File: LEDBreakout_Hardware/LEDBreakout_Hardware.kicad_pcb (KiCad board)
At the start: 2 copper layers, 39.9 x 39.9 mm, 29 parts, among them Q1 BSS138, Q2 BSS138, Q3 BSS138, Q4 BSS138

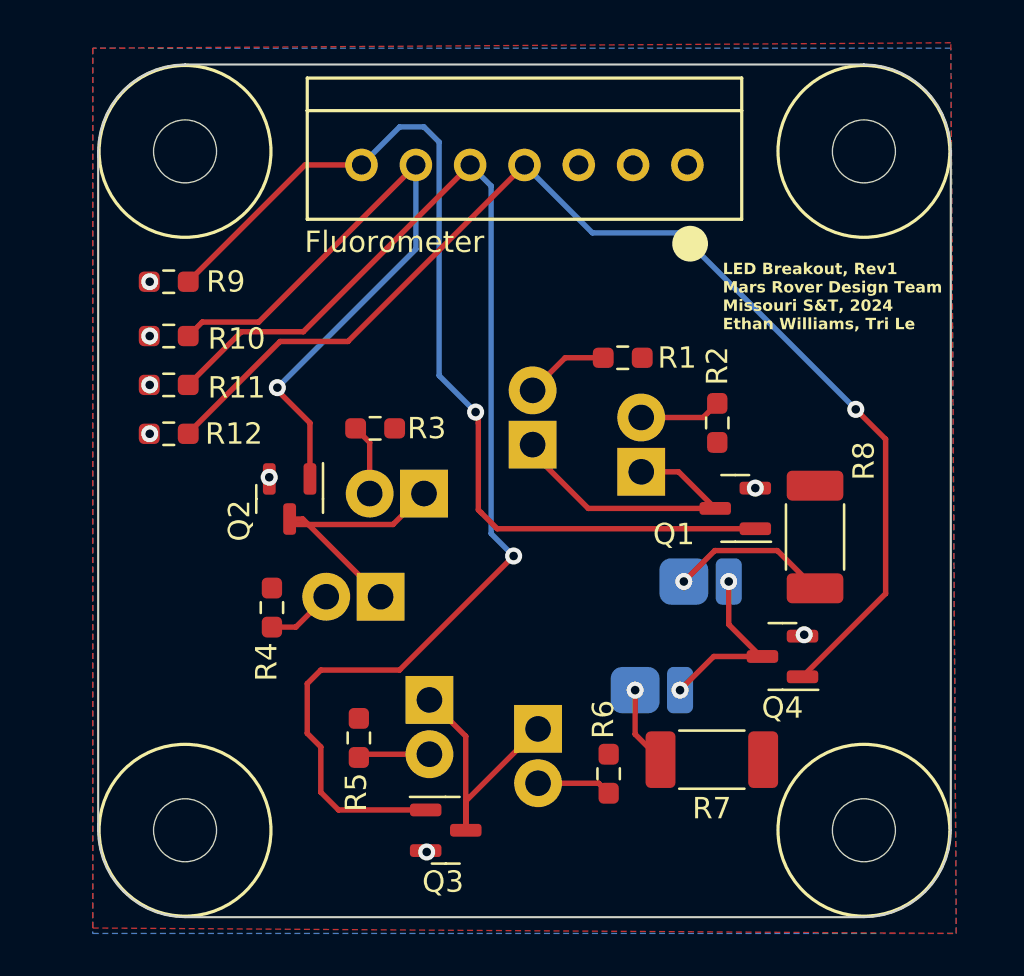
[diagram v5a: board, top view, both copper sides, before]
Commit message: Moved Vias off pads
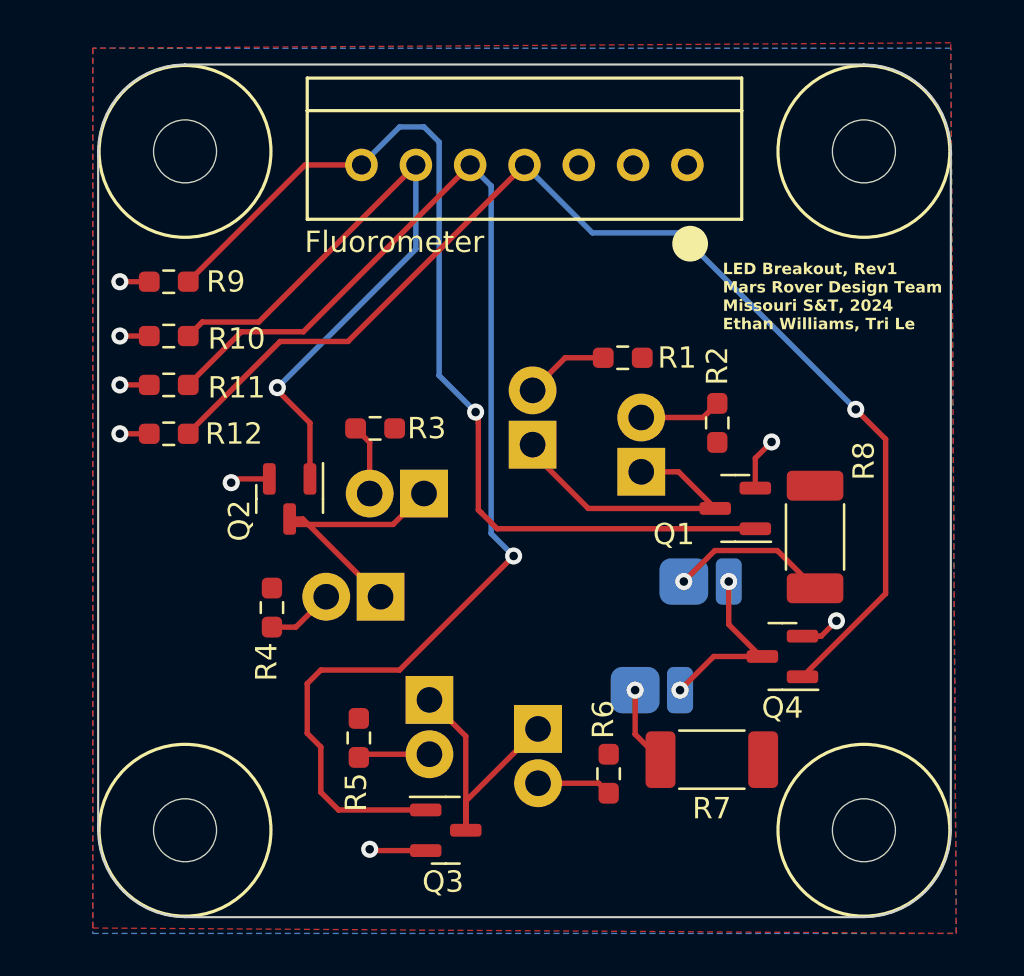
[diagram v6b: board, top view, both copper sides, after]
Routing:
- net GND: track 0.00 -> 14.4 mm
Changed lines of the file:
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@@
   (segment (start 84.836 74.676) (end 86.36 73.152) (width 0.254) (layer "F.Cu") (net 1))
   (segment (start 86.36 73.152) (end 88.138 73.152) (width 0.254) (layer "F.Cu") (net 1))
-  (via (at 95.25 79.248) (size 0.8) (drill 0.4) (layers "F.Cu" "B.Cu") (net 2))
-  (via (at 97.536 86.106) (size 0.8) (drill 0.4) (layers "F.Cu" "B.Cu") (net 2))
-  (via (at 79.883 96.266) (size 0.8) (drill 0.4) (layers "F.Cu" "B.Cu") (net 2))
-  (via (at 66.929 74.422) (size 0.8) (drill 0.4) (layers "F.Cu" "B.Cu") (net 2))
-  (via (at 66.929 76.708) (size 0.8) (drill 0.4) (layers "F.Cu" "B.Cu") (net 2))
-  (via (at 66.929 72.136) (size 0.8) (drill 0.4) (layers "F.Cu" "B.Cu") (net 2))
-  (via (at 66.929 69.596) (size 0.8) (drill 0.4) (layers "F.Cu" "B.Cu") (net 2))
-  (via (at 72.517 78.74) (size 0.8) (drill 0.4) (layers "F.Cu" "B.Cu") (net 2))
+  (segment (start 66.9055 72.136) (end 65.532 72.136) (width 0.25) (layer "F.Cu") (net 2))
+  (segment (start 66.9055 76.708) (end 65.532 76.708) (width 0.25) (layer "F.Cu") (net 2))
+  (segment (start 97.4575 86.172) (end 98.330072 86.172) (width 0.25) (layer "F.Cu") (net 2))
+  (segment (start 70.9145 78.8185) (end 70.739 78.994) (width 0.25) (layer "F.Cu") (net 2))
+  (segment (start 66.9055 74.422) (end 65.532 74.422) (width 0.25) (layer "F.Cu") (net 2))
+  (segment (start 72.522 78.8185) (end 70.9145 78.8185) (width 0.25) (layer "F.Cu") (net 2))
+  (segment (start 98.330072 86.172) (end 99.045536 85.456536) (width 0.25) (layer "F.Cu") (net 2))
+  (segment (start 79.8345 96.2) (end 77.277 96.2) (width 0.25) (layer "F.Cu") (net 2))
+  (segment (start 95.25 77.851) (end 96.012 77.089) (width 0.25) (layer "F.Cu") (net 2))
+  (segment (start 66.9055 69.596) (end 65.532 69.596) (width 0.25) (layer "F.Cu") (net 2))
+  (segment (start 95.25 79.248) (end 95.25 77.851) (width 0.25) (layer "F.Cu") (net 2))
+  (segment (start 77.277 96.2) (end 77.216 96.139) (width 0.25) (layer "F.Cu") (net 2))
+  (via (at 65.532 69.596) (size 0.8) (drill 0.4) (layers "F.Cu" "B.Cu") (net 2))
+  (via (at 99.045536 85.456536) (size 0.8) (drill 0.4) (layers "F.Cu" "B.Cu") (net 2))
+  (via (at 65.532 76.708) (size 0.8) (drill 0.4) (layers "F.Cu" "B.Cu") (net 2))
+  (via (at 65.532 74.422) (size 0.8) (drill 0.4) (layers "F.Cu" "B.Cu") (net 2))
+  (via (at 77.216 96.139) (size 0.8) (drill 0.4) (layers "F.Cu" "B.Cu") (net 2))
+  (via (at 96.012 77.089) (size 0.8) (drill 0.4) (layers "F.Cu" "B.Cu") (net 2))
+  (via (at 65.532 72.136) (size 0.8) (drill 0.4) (layers "F.Cu" "B.Cu") (net 2))
+  (via (at 70.739 78.994) (size 0.8) (drill 0.4) (layers "F.Cu" "B.Cu") (net 2))
   (segment (start 93.375 80.198) (end 87.437 80.198) (width 0.254) (layer "F.Cu") (net 3))
   (segment (start 91.663 78.486) (end 89.916 78.486) (width 0.254) (layer "F.Cu") (net 3))
